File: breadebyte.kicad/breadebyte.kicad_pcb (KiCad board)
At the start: 2 copper layers, 23.9 x 52 mm, 7 parts, among them J1 USB_B_Micro, J2 Conn_Left, J3 Conn_Right, J4 SWD, U1 E73-2G4M08S1E

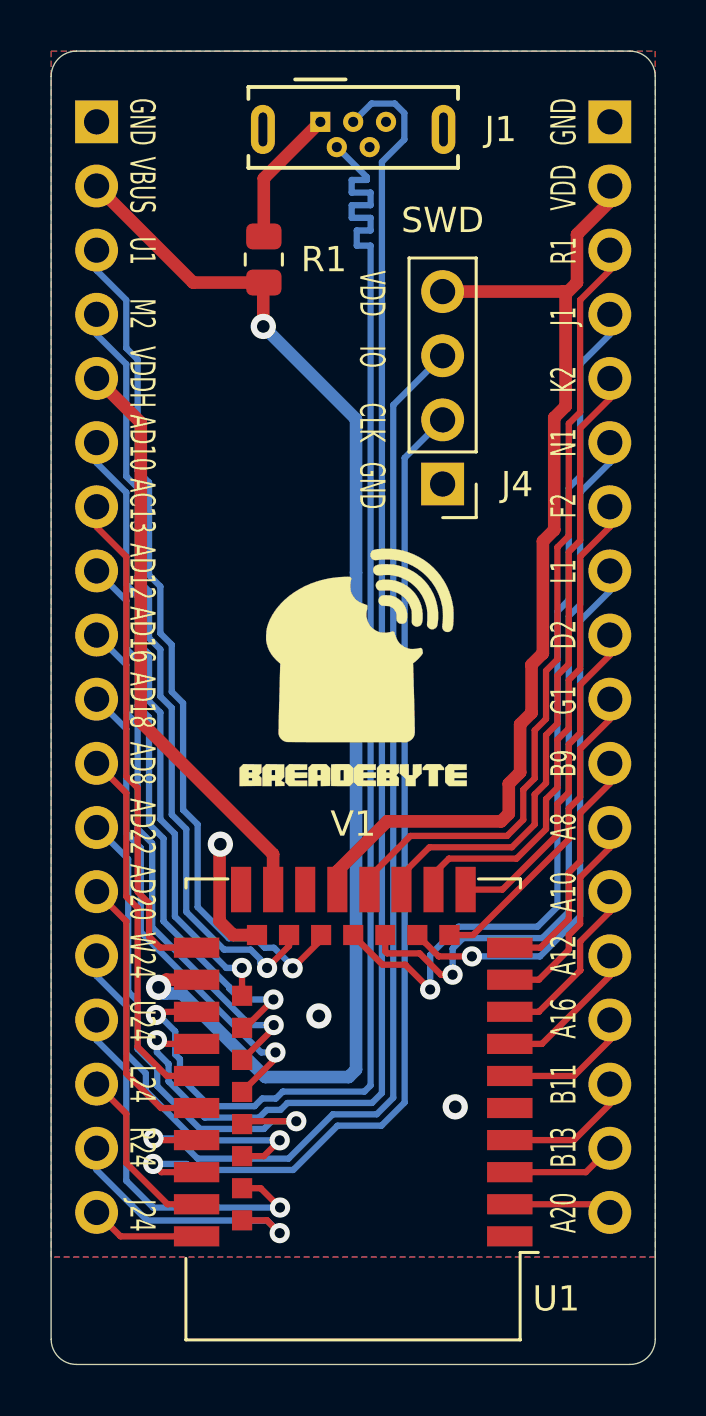
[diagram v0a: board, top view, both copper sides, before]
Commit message: Upgrade KiCAD project to KiCAD v6
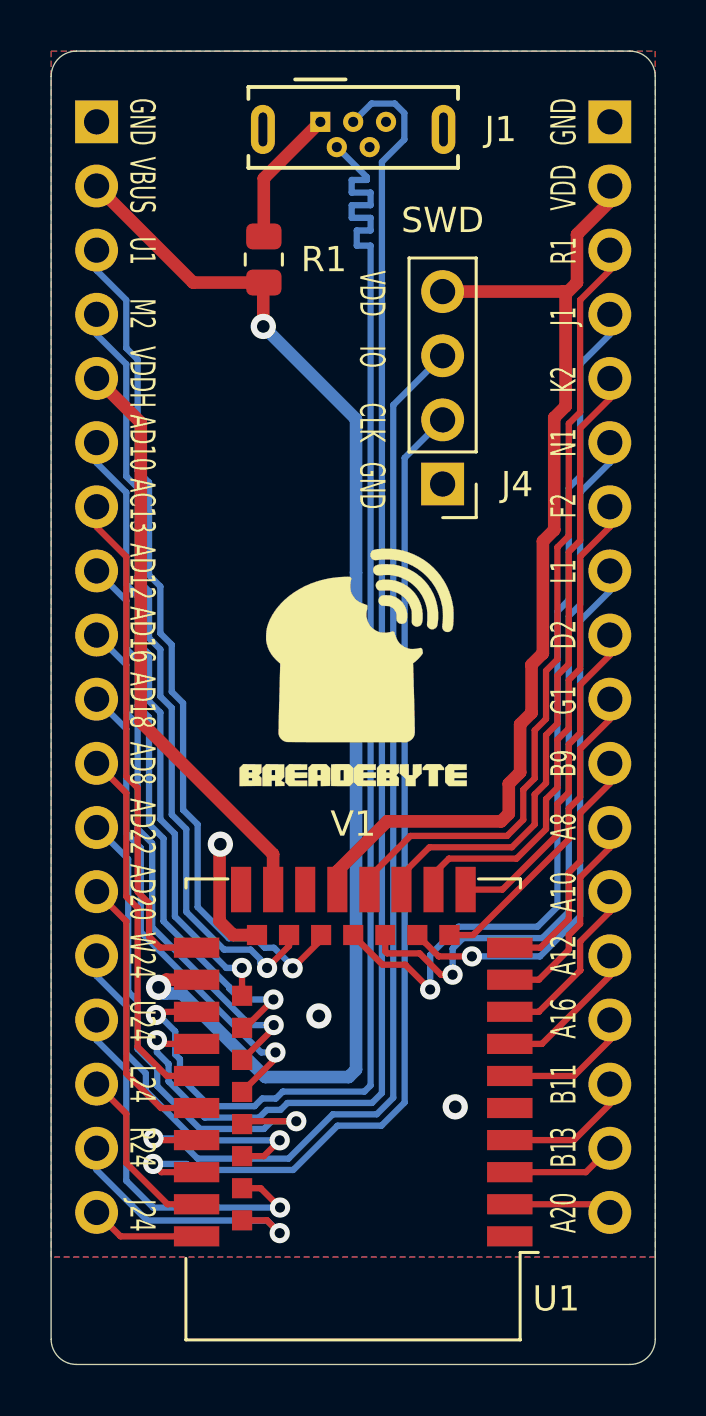
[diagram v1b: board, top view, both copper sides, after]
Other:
- net class Default removed

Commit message: Switch to using shared symbol/footprint library
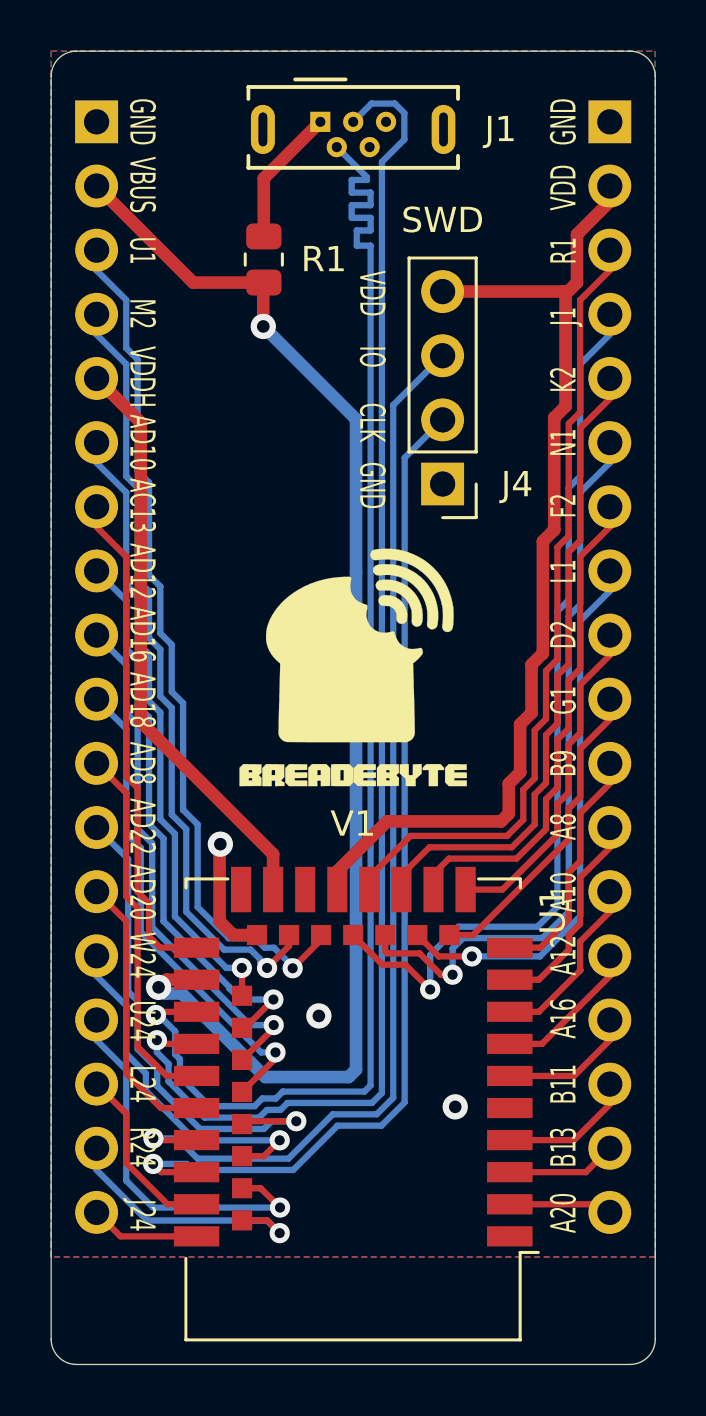
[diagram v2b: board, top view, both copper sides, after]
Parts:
- U1: footprint breadebyte:E73-2G4M08S1E -> spbnick:E73-2G4M08S1E
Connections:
- J1 pad 4: Net-(J1-Pad4) -> unconnected-(J1-Pad4)
- J1 pad 6: Net-(J1-Pad6) -> unconnected-(J1-Pad6)
- U1 pad 1: Net-(U1-Pad1) -> unconnected-(U1-Pad1)
- U1 pad 25: Net-(U1-Pad25) -> unconnected-(U1-Pad25)
